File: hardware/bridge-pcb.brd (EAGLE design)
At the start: 82.5 x 33 mm, 22 parts, among them IC1 MC34063AP, IC2 MAX3232CPE, J1 RJ11, J2 RJ9PTH, M1 ESP01

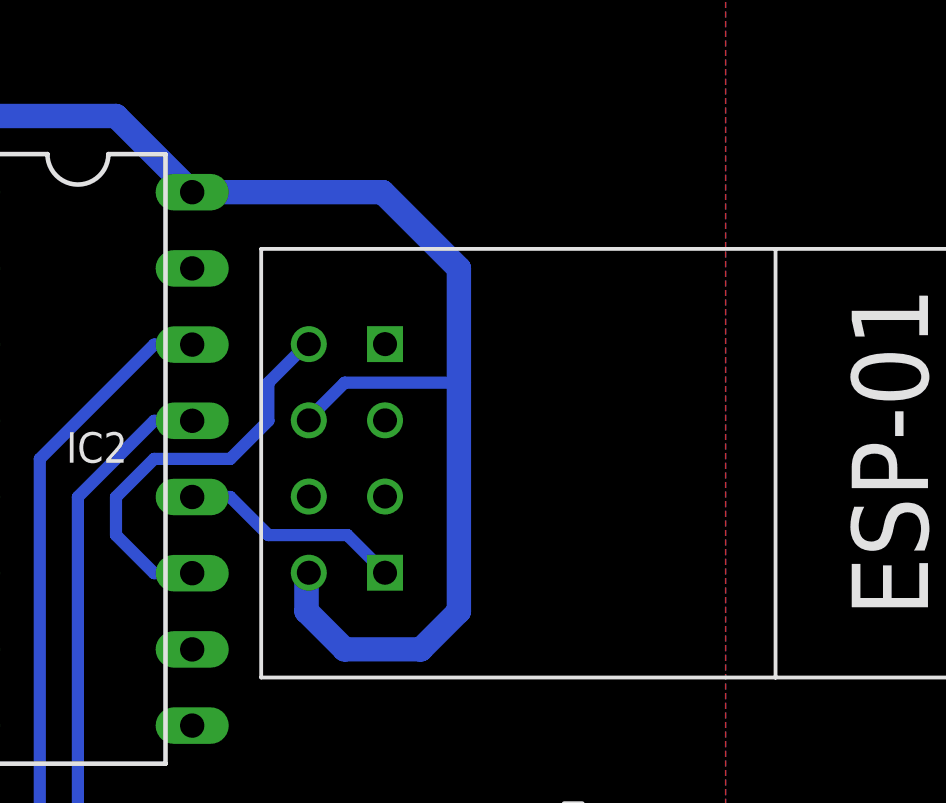
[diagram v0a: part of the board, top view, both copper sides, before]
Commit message: Added pin header footprint to provide support for the ESP8266 module
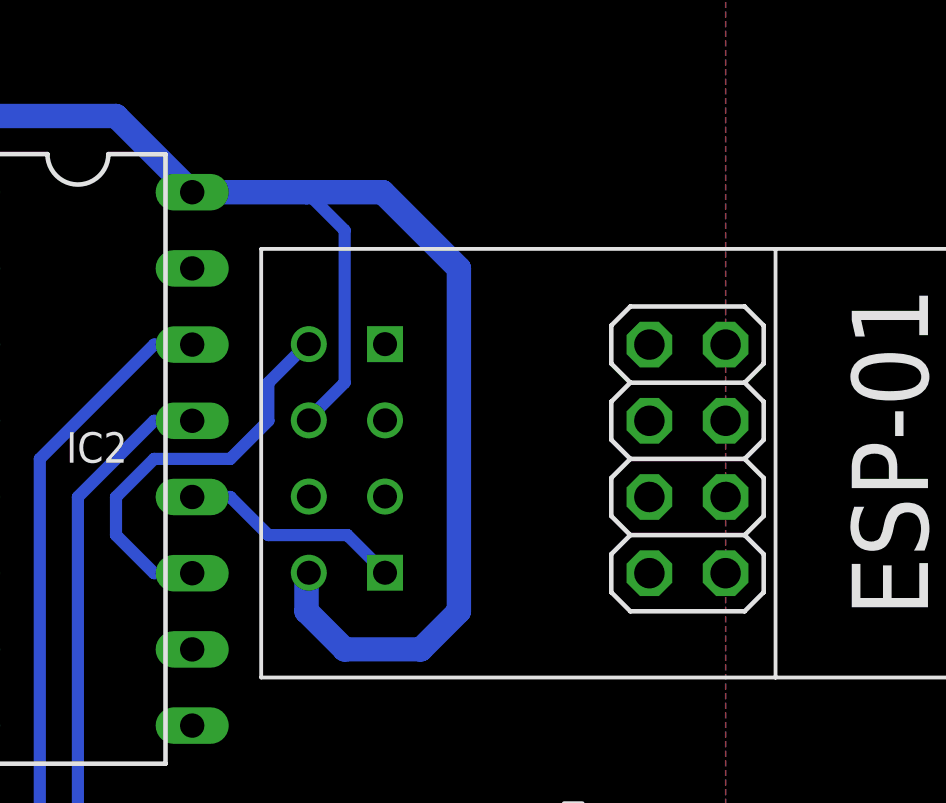
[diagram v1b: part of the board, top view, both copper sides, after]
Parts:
- added SV1: (no value), pinhead:2X04
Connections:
- net GND: now also SV1.1, SV1.2, SV1.3, SV1.4, SV1.5, SV1.6, SV1.7, SV1.8
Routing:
- net 3V3: track 96.8 -> 99.9 mm
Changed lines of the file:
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@@
 </classes>
 <designrules name="oshpark-2layer">
-<description language="de">&lt;b&gt;EAGLE Design Rules&lt;/b&gt;
+<description language="en">&lt;b&gt;OSH Park Design Rules&lt;/b&gt;
 &lt;p&gt;
-Die Standard-Design-Rules sind so gewählt, dass sie für
-die meisten Anwendungen passen. Sollte ihre Platine
-besondere Anforderungen haben, treffen Sie die erforderlichen
-Einstellungen hier und speichern die Design Rules unter
-einem neuen Namen ab.</description>
-<description language="en">&lt;b&gt;Laen's PCB Order Design Rules&lt;/b&gt;
+Please make sure your boards conform to these design rules.
+&lt;/p&gt;
 &lt;p&gt;
-Please make sure your boards conform to these design rules.</description>
+Note, that not all DRC settings must be set by the manufacturer. Several can be adjusted for the design, including those listed on our docs page here.
+&lt;a href=&quot;http://docs.oshpark.com/design-tools/eagle/design-rules-files/&quot;&gt;Adjustable Settings&lt;/a&gt;
+&lt;/p&gt;</description>
 <param name="layerSetup" value="(1*16)"/>
-<param name="mtCopper" value="0.0356mm 0.0356mm 0.0356mm 0.0356mm 0.0356mm 0.0356mm 0.0356mm 0.0356mm 0.0356mm 0.0356mm 0.0356mm 0.0356mm 0.0356mm 0.0356mm 0.0356mm 0.0356mm"/>
-<param name="mtIsolate" value="1.5011mm 0.1499mm 0.2007mm 0.1499mm 0.2007mm 0.1499mm 0.2007mm 0.1499mm 0.2007mm 0.1499mm 0.2007mm 0.1499mm 0.2007mm 0.1499mm 0.2007mm"/>
+<param name="mtCopper" value="0.035559375mm 0.0356mm 0.0356mm 0.0356mm 0.0356mm 0.0356mm 0.0356mm 0.0356mm 0.0356mm 0.0356mm 0.0356mm 0.0356mm 0.0356mm 0.0356mm 0.0356mm 0.035559375mm"/>
+<param name="mtIsolate" value="1.6mm 0.1499mm 0.2007mm 0.1499mm 0.2007mm 0.1499mm 0.2007mm 0.1499mm 0.2007mm 0.1499mm 0.2007mm 0.1499mm 0.2007mm 0.1499mm 0.2007mm"/>
 <param name="mdWireWire" value="6mil"/>
 <param name="mdWirePad" value="6mil"/>
@@
 <param name="mdSmdStop" value="0mil"/>
 <param name="msWidth" value="6mil"/>
-<param name="msDrill" value="13mil"/>
-<param name="msMicroVia" value="13mil"/>
+<param name="msDrill" value="10mil"/>
+<param name="msMicroVia" value="10mil"/>
 <param name="msBlindViaRatio" value="0.5"/>
 <param name="rvPadTop" value="0.25"/>
@@
 <param name="rvMicroViaOuter" value="0.25"/>
 <param name="rvMicroViaInner" value="0.25"/>
-<param name="rlMinPadTop" value="7mil"/>
+<param name="rlMinPadTop" value="5mil"/>
 <param name="rlMaxPadTop" value="20mil"/>
-<param name="rlMinPadInner" value="7mil"/>
+<param name="rlMinPadInner" value="5mil"/>
 <param name="rlMaxPadInner" value="20mil"/>
-<param name="rlMinPadBottom" value="7mil"/>
+<param name="rlMinPadBottom" value="5mil"/>
 <param name="rlMaxPadBottom" value="20mil"/>
-<param name="rlMinViaOuter" value="7mil"/>
+<param name="rlMinViaOuter" value="5mil"/>
 <param name="rlMaxViaOuter" value="20mil"/>
-<param name="rlMinViaInner" value="7mil"/>
+<param name="rlMinViaInner" value="5mil"/>
 <param name="rlMaxViaInner" value="20mil"/>
-<param name="rlMinMicroViaOuter" value="4mil"/>
+<param name="rlMinMicroViaOuter" value="5mil"/>
 <param name="rlMaxMicroViaOuter" value="20mil"/>
-<param name="rlMinMicroViaInner" value="4mil"/>
+<param name="rlMinMicroViaInner" value="5mil"/>
 <param name="rlMaxMicroViaInner" value="20mil"/>
 <param name="psTop" value="-1"/>
@@
 </element>
 <element name="M1" library="esp8266modules" package="ESP01" value="ESP01" x="66.675" y="16.51" smashed="yes" rot="R270">
-<attribute name="VALUE" x="64.12" y="15.67" size="1.016" layer="27" ratio="10"/>
+<attribute name="VALUE" x="64.12" y="10.59" size="1.016" layer="27" ratio="10"/>
 </element>
 <element name="C6" library="rcl" package="C025-024X044" value="0.1u" x="43.18" y="12.7" smashed="yes" rot="R180">
@@
 </element>
 <element name="LOGO1" library="SparkFun-Aesthetics" package="OSHW-LOGO-M" value="OSHW-LOGOM" x="67.31" y="2.54"/>
+<element name="SV1" library="pinhead" package="2X04" value="" x="71.12" y="16.51" smashed="yes" rot="R90">
+<attribute name="VALUE" x="75.311" y="16.51" size="1.27" layer="27" ratio="10" rot="R90"/>
+</element>
 </elements>
 <signals>
@@
 <vertex x="0" y="0"/>
 </polygon>
+<contactref element="SV1" pad="8"/>
+<contactref element="SV1" pad="7"/>
+<contactref element="SV1" pad="2"/>
+<contactref element="SV1" pad="4"/>
+<contactref element="SV1" pad="6"/>
+<contactref element="SV1" pad="5"/>
+<contactref element="SV1" pad="3"/>
+<contactref element="SV1" pad="1"/>
 </signal>
 <signal name="12V" class="1">
@@
 <wire x1="20.32" y1="30.48" x2="34.25" y2="30.48" width="0.8128" layer="16"/>
 <wire x1="34.25" y1="30.48" x2="36.79" y2="27.94" width="0.8128" layer="16"/>
-<wire x1="54.61" y1="25.4" x2="60.96" y2="25.4" width="0.8128" layer="16"/>
+<wire x1="54.61" y1="25.4" x2="58.42" y2="25.4" width="0.8128" layer="16"/>
+<wire x1="58.42" y1="25.4" x2="60.96" y2="25.4" width="0.8128" layer="16"/>
 <wire x1="60.96" y1="25.4" x2="63.5" y2="22.86" width="0.8128" layer="16"/>
-<wire x1="63.5" y1="22.86" x2="63.5" y2="19.05" width="0.8128" layer="16"/>
-<wire x1="63.5" y1="19.05" x2="63.5" y2="11.43" width="0.8128" layer="16"/>
+<wire x1="63.5" y1="22.86" x2="63.5" y2="11.43" width="0.8128" layer="16"/>
 <wire x1="63.5" y1="11.43" x2="62.23" y2="10.16" width="0.8128" layer="16"/>
 <wire x1="62.23" y1="10.16" x2="59.69" y2="10.16" width="0.8128" layer="16"/>
@@
 <wire x1="58.4975" y1="17.795" x2="58.4975" y2="17.8575" width="0.8128" layer="16"/>
 <wire x1="58.4975" y1="17.8575" x2="59.69" y2="19.05" width="0.4064" layer="16"/>
-<wire x1="59.69" y1="19.05" x2="63.5" y2="19.05" width="0.4064" layer="16"/>
+<wire x1="59.69" y1="19.05" x2="59.69" y2="24.13" width="0.4064" layer="16"/>
+<wire x1="59.69" y1="24.13" x2="58.42" y2="25.4" width="0.4064" layer="16"/>
 </signal>
 <signal name="N$5">
